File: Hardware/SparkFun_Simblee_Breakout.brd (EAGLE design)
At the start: 22.9 x 58.4 mm, 24 parts, among them U1 ADP160, U2 RFD77101

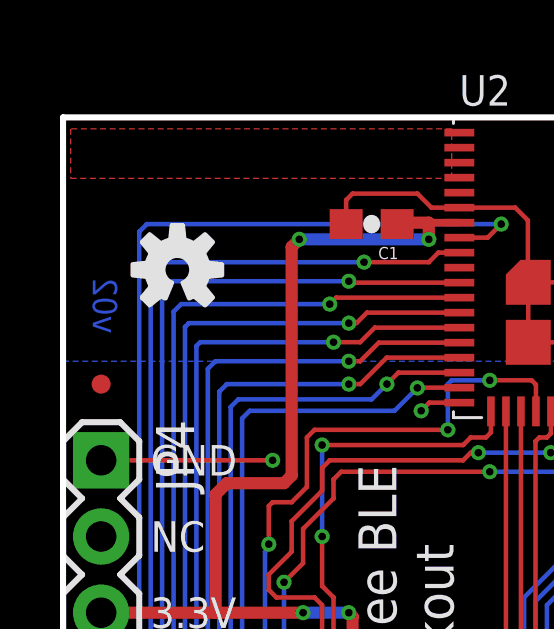
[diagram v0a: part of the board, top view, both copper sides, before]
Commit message: Update to v10. Chg gnd pad to 12.5% paste
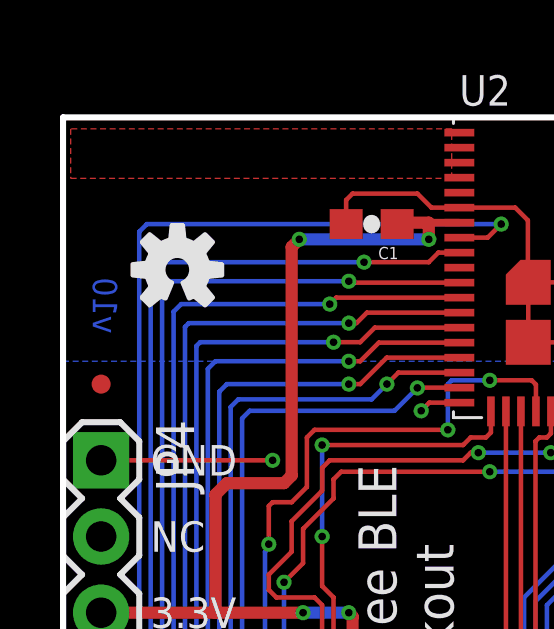
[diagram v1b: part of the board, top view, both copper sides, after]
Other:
- board text added: "v10"
- board text removed: "v02"
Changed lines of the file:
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@@
 <layers>
 <layer number="1" name="Top" color="4" fill="1" visible="yes" active="yes"/>
-<layer number="2" name="Route2" color="1" fill="3" visible="no" active="yes"/>
-<layer number="15" name="Route15" color="4" fill="6" visible="no" active="yes"/>
+<layer number="2" name="Route2" color="1" fill="3" visible="yes" active="yes"/>
+<layer number="15" name="Route15" color="4" fill="6" visible="yes" active="yes"/>
 <layer number="16" name="Bottom" color="1" fill="1" visible="yes" active="yes"/>
 <layer number="17" name="Pads" color="2" fill="1" visible="yes" active="yes"/>
@@
 <layer number="23" name="tOrigins" color="15" fill="1" visible="yes" active="yes"/>
 <layer number="24" name="bOrigins" color="15" fill="1" visible="yes" active="yes"/>
-<layer number="25" name="tNames" color="7" fill="1" visible="no" active="yes"/>
-<layer number="26" name="bNames" color="7" fill="1" visible="no" active="yes"/>
-<layer number="27" name="tValues" color="7" fill="1" visible="no" active="yes"/>
-<layer number="28" name="bValues" color="7" fill="1" visible="no" active="yes"/>
-<layer number="29" name="tStop" color="7" fill="3" visible="no" active="yes"/>
-<layer number="30" name="bStop" color="7" fill="6" visible="no" active="yes"/>
-<layer number="31" name="tCream" color="7" fill="4" visible="no" active="yes"/>
-<layer number="32" name="bCream" color="7" fill="5" visible="no" active="yes"/>
-<layer number="39" name="tKeepout" color="4" fill="11" visible="no" active="yes"/>
-<layer number="40" name="bKeepout" color="1" fill="11" visible="no" active="yes"/>
-<layer number="41" name="tRestrict" color="4" fill="10" visible="no" active="yes"/>
-<layer number="42" name="bRestrict" color="1" fill="10" visible="no" active="yes"/>
-<layer number="43" name="vRestrict" color="2" fill="10" visible="no" active="yes"/>
-<layer number="44" name="Drills" color="7" fill="1" visible="no" active="yes"/>
+<layer number="25" name="tNames" color="7" fill="1" visible="yes" active="yes"/>
+<layer number="26" name="bNames" color="7" fill="1" visible="yes" active="yes"/>
+<layer number="27" name="tValues" color="7" fill="1" visible="yes" active="yes"/>
+<layer number="28" name="bValues" color="7" fill="1" visible="yes" active="yes"/>
+<layer number="29" name="tStop" color="7" fill="3" visible="yes" active="yes"/>
+<layer number="30" name="bStop" color="7" fill="6" visible="yes" active="yes"/>
+<layer number="31" name="tCream" color="7" fill="4" visible="yes" active="yes"/>
+<layer number="32" name="bCream" color="7" fill="5" visible="yes" active="yes"/>
+<layer number="39" name="tKeepout" color="4" fill="11" visible="yes" active="yes"/>
+<layer number="40" name="bKeepout" color="1" fill="11" visible="yes" active="yes"/>
+<layer number="41" name="tRestrict" color="4" fill="10" visible="yes" active="yes"/>
+<layer number="42" name="bRestrict" color="1" fill="10" visible="yes" active="yes"/>
+<layer number="43" name="vRestrict" color="2" fill="10" visible="yes" active="yes"/>
+<layer number="44" name="Drills" color="7" fill="1" visible="yes" active="yes"/>
 <layer number="45" name="Holes" color="7" fill="1" visible="yes" active="yes"/>
-<layer number="46" name="Milling" color="3" fill="1" visible="no" active="yes"/>
-<layer number="47" name="Measures" color="7" fill="1" visible="no" active="yes"/>
+<layer number="46" name="Milling" color="3" fill="1" visible="yes" active="yes"/>
+<layer number="47" name="Measures" color="7" fill="1" visible="yes" active="yes"/>
 <layer number="51" name="tDocu" color="6" fill="1" visible="yes" active="yes"/>
 <layer number="50" name="dxf" color="7" fill="1" visible="no" active="no"/>
@@
 <text x="11.43" y="29.21" size="1.27" layer="22" font="vector" ratio="15" rot="MR270" align="center-left">Simblee BLE
 Breakout</text>
-<text x="1.397" y="53.086" size="0.8128" layer="16" font="vector" ratio="15" rot="MR270" align="center-left">v02</text>
+<text x="1.397" y="53.086" size="0.8128" layer="16" font="vector" ratio="15" rot="MR270" align="center-left">v10</text>
 <text x="30.48" y="-20.32" size="1.778" layer="51" font="vector" ratio="15">Mike Hord</text>
 <rectangle x1="12.3698" y1="56.4896" x2="12.7" y2="57.3278" layer="41"/>
@@
 </class>
 </classes>
-<designrules name="Gold_Phoenix_Standard_Spec_2_layer *">
-<description language="en">&lt;b&gt;EAGLE Design Rules&lt;/b&gt;
-&lt;p&gt;
-The default Design Rules have been set to cover
-a wide range of applications. Your particular design
-may have different requirements, so please make the
-necessary adjustments and save your customized
-design rules under a new name.</description>
+<designrules name="SparkFun-2-layer-FAB-LIMIT">
+<description language="en">&lt;b&gt;SparkFun 2 Layer Design Rule Checks - STANDARD/TIGHT/FAB-LIMIT&lt;/b&gt;
+&lt;p&gt;
+These rules have been curated by SparkFuns DFM commitee. After doing much research, communicating with our multiple fab houses, and getting quotes of various designs, we have compiled three DRU files.
+&lt;p&gt;
+&lt;b&gt;STANDARD:&lt;/b&gt; This is more of a &quot;best case scenario&quot; set of limitations. If your design has the space, and/or you have the time to work within these parameters, please do. Larger trace width and clearance makes for easier visual inspection of the PCB while troubleshooting (useful in production and to the end user). It also allows for better ability to hack a trace (if you are crazy enough to scrape away the mask and solder to a trace). Another thing to keep in mind is that more metal is just more robust.
+&lt;p&gt;
+&lt;b&gt;TIGHT:&lt;/b&gt; This is where cost comes into play. We have found that most fab houses begin to add extra charges when you go smaller than these specs. In some cases, going to less than 15 mil trace can increase the cost by 10%. (This is why we have set the min drill on this DRU to 15 mil) Same story for traces thinner than 7 mil. To avoid those extra charges, then stay within the rules of this DRU.
+&lt;p&gt;
+&lt;b&gt;FAB-LIMIT:&lt;/b&gt; These set of rules are at the very limit of most fab houses capabilities. You will pay more for these specs, and it should be used on designs that have a darned good reason to need 4 mil vias and 4 mil traces.
+&lt;p&gt;
+**NOTE Clearance, Distance, Sizes, and Restring are all set to different limits in each of these three DRU files. Please compare the files within the CAM job editor window of eagle to see all the numbers.
+&lt;p&gt;
+***NOTE, Please set your Net Classes to default (0mil for all settings), so that it won't effect the DRC when you run it with these settings.</description>
 <param name="layerSetup" value="(1*16)"/>
 <param name="mtCopper" value="0.035mm 0.035mm 0.035mm 0.035mm 0.035mm 0.035mm 0.035mm 0.035mm 0.035mm 0.035mm 0.035mm 0.035mm 0.035mm 0.035mm 0.035mm 0.035mm"/>
 <param name="mtIsolate" value="1.5mm 0.15mm 0.2mm 0.15mm 0.2mm 0.15mm 0.2mm 0.15mm 0.2mm 0.15mm 0.2mm 0.15mm 0.2mm 0.15mm 0.2mm"/>
-<param name="mdWireWire" value="7mil"/>
-<param name="mdWirePad" value="7mil"/>
-<param name="mdWireVia" value="7mil"/>
-<param name="mdPadPad" value="7mil"/>
-<param name="mdPadVia" value="7mil"/>
-<param name="mdViaVia" value="7mil"/>
-<param name="mdSmdPad" value="5mil"/>
-<param name="mdSmdVia" value="5mil"/>
-<param name="mdSmdSmd" value="5mil"/>
+<param name="mdWireWire" value="4mil"/>
+<param name="mdWirePad" value="4mil"/>
+<param name="mdWireVia" value="4mil"/>
+<param name="mdPadPad" value="4mil"/>
+<param name="mdPadVia" value="4mil"/>
+<param name="mdViaVia" value="4mil"/>
+<param name="mdSmdPad" value="4mil"/>
+<param name="mdSmdVia" value="4mil"/>
+<param name="mdSmdSmd" value="4mil"/>
 <param name="mdViaViaSameLayer" value="8mil"/>
 <param name="mnLayersViaInSmd" value="2"/>
-<param name="mdCopperDimension" value="8mil"/>
-<param name="mdDrill" value="8mil"/>
+<param name="mdCopperDimension" value="4mil"/>
+<param name="mdDrill" value="4mil"/>
 <param name="mdSmdStop" value="0mil"/>
-<param name="msWidth" value="5mil"/>
+<param name="msWidth" value="4mil"/>
 <param name="msDrill" value="6mil"/>
 <param name="msMicroVia" value="9.99mm"/>
@@
 <param name="rlMinPadTop" value="5mil"/>
 <param name="rlMaxPadTop" value="20mil"/>
-<param name="rlMinPadInner" value="10mil"/>
+<param name="rlMinPadInner" value="6mil"/>
 <param name="rlMaxPadInner" value="20mil"/>
 <param name="rlMinPadBottom" value="5mil"/>
@@
 <param name="rlMinViaOuter" value="5mil"/>
 <param name="rlMaxViaOuter" value="20mil"/>
-<param name="rlMinViaInner" value="10mil"/>
+<param name="rlMinViaInner" value="6mil"/>
 <param name="rlMaxViaInner" value="20mil"/>
 <param name="rlMinMicroViaOuter" value="4mil"/>

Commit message: Rotate SF logo on bottom, ver to 11
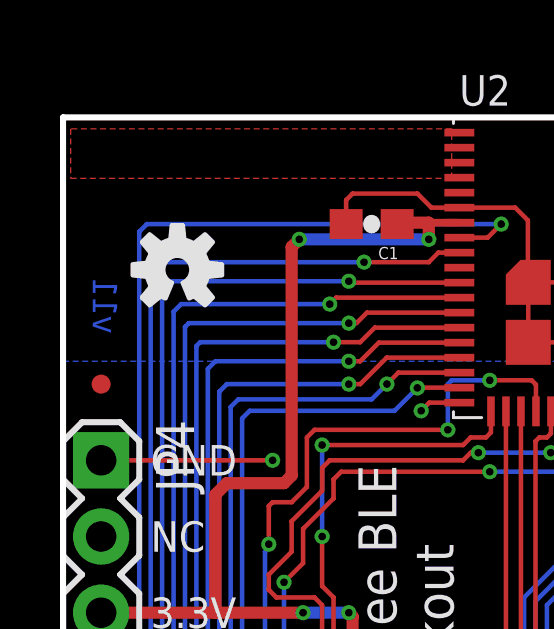
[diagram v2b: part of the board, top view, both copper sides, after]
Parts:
- moved LOGO3 13.7 mm to (13.6, 16.6), turned to 90 degrees
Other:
- board text added: "v11"
- board text removed: "v10"
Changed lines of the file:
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@@
 <grid distance="0.05" unitdist="inch" unit="inch" style="lines" multiple="1" display="yes" altdistance="0.005" altunitdist="inch" altunit="inch"/>
 <layers>
-<layer number="1" name="Top" color="4" fill="1" visible="yes" active="yes"/>
-<layer number="2" name="Route2" color="1" fill="3" visible="yes" active="yes"/>
-<layer number="15" name="Route15" color="4" fill="6" visible="yes" active="yes"/>
+<layer number="1" name="Top" color="4" fill="1" visible="no" active="yes"/>
+<layer number="2" name="Route2" color="1" fill="3" visible="no" active="yes"/>
+<layer number="15" name="Route15" color="4" fill="6" visible="no" active="yes"/>
 <layer number="16" name="Bottom" color="1" fill="1" visible="yes" active="yes"/>
 <layer number="17" name="Pads" color="2" fill="1" visible="yes" active="yes"/>
@@
 <layer number="19" name="Unrouted" color="6" fill="1" visible="yes" active="yes"/>
 <layer number="20" name="Dimension" color="15" fill="1" visible="yes" active="yes"/>
-<layer number="21" name="tPlace" color="16" fill="1" visible="yes" active="yes"/>
+<layer number="21" name="tPlace" color="16" fill="1" visible="no" active="yes"/>
 <layer number="22" name="bPlace" color="14" fill="1" visible="yes" active="yes"/>
-<layer number="23" name="tOrigins" color="15" fill="1" visible="yes" active="yes"/>
+<layer number="23" name="tOrigins" color="15" fill="1" visible="no" active="yes"/>
 <layer number="24" name="bOrigins" color="15" fill="1" visible="yes" active="yes"/>
-<layer number="25" name="tNames" color="7" fill="1" visible="yes" active="yes"/>
-<layer number="26" name="bNames" color="7" fill="1" visible="yes" active="yes"/>
-<layer number="27" name="tValues" color="7" fill="1" visible="yes" active="yes"/>
-<layer number="28" name="bValues" color="7" fill="1" visible="yes" active="yes"/>
-<layer number="29" name="tStop" color="7" fill="3" visible="yes" active="yes"/>
-<layer number="30" name="bStop" color="7" fill="6" visible="yes" active="yes"/>
-<layer number="31" name="tCream" color="7" fill="4" visible="yes" active="yes"/>
-<layer number="32" name="bCream" color="7" fill="5" visible="yes" active="yes"/>
-<layer number="39" name="tKeepout" color="4" fill="11" visible="yes" active="yes"/>
-<layer number="40" name="bKeepout" color="1" fill="11" visible="yes" active="yes"/>
-<layer number="41" name="tRestrict" color="4" fill="10" visible="yes" active="yes"/>
-<layer number="42" name="bRestrict" color="1" fill="10" visible="yes" active="yes"/>
-<layer number="43" name="vRestrict" color="2" fill="10" visible="yes" active="yes"/>
-<layer number="44" name="Drills" color="7" fill="1" visible="yes" active="yes"/>
-<layer number="45" name="Holes" color="7" fill="1" visible="yes" active="yes"/>
-<layer number="46" name="Milling" color="3" fill="1" visible="yes" active="yes"/>
-<layer number="47" name="Measures" color="7" fill="1" visible="yes" active="yes"/>
-<layer number="51" name="tDocu" color="6" fill="1" visible="yes" active="yes"/>
+<layer number="25" name="tNames" color="7" fill="1" visible="no" active="yes"/>
+<layer number="26" name="bNames" color="7" fill="1" visible="no" active="yes"/>
+<layer number="27" name="tValues" color="7" fill="1" visible="no" active="yes"/>
+<layer number="28" name="bValues" color="7" fill="1" visible="no" active="yes"/>
+<layer number="29" name="tStop" color="7" fill="3" visible="no" active="yes"/>
+<layer number="30" name="bStop" color="7" fill="6" visible="no" active="yes"/>
+<layer number="31" name="tCream" color="7" fill="4" visible="no" active="yes"/>
+<layer number="32" name="bCream" color="7" fill="5" visible="no" active="yes"/>
+<layer number="39" name="tKeepout" color="4" fill="11" visible="no" active="yes"/>
+<layer number="40" name="bKeepout" color="1" fill="11" visible="no" active="yes"/>
+<layer number="41" name="tRestrict" color="4" fill="10" visible="no" active="yes"/>
+<layer number="42" name="bRestrict" color="1" fill="10" visible="no" active="yes"/>
+<layer number="43" name="vRestrict" color="2" fill="10" visible="no" active="yes"/>
+<layer number="44" name="Drills" color="7" fill="1" visible="no" active="yes"/>
+<layer number="45" name="Holes" color="7" fill="1" visible="no" active="yes"/>
+<layer number="46" name="Milling" color="3" fill="1" visible="no" active="yes"/>
+<layer number="47" name="Measures" color="7" fill="1" visible="no" active="yes"/>
+<layer number="51" name="tDocu" color="6" fill="1" visible="no" active="yes"/>
 <layer number="50" name="dxf" color="7" fill="1" visible="no" active="no"/>
 <layer number="3" name="Route3" color="4" fill="3" visible="no" active="no"/>
@@
 <text x="11.43" y="29.21" size="1.27" layer="22" font="vector" ratio="15" rot="MR270" align="center-left">Simblee BLE
 Breakout</text>
-<text x="1.397" y="53.086" size="0.8128" layer="16" font="vector" ratio="15" rot="MR270" align="center-left">v10</text>
+<text x="1.397" y="53.086" size="0.8128" layer="16" font="vector" ratio="15" rot="MR270" align="center-left">v11</text>
 <text x="30.48" y="-20.32" size="1.778" layer="51" font="vector" ratio="15">Mike Hord</text>
 <rectangle x1="12.3698" y1="56.4896" x2="12.7" y2="57.3278" layer="41"/>
@@
 <element name="LOGO1" library="SparkFun-Aesthetics" package="SFE_LOGO_NAME_.1" value="SFE_LOGO_NAME.1_INCH" x="8.763" y="19.05" rot="R90"/>
 <element name="LOGO2" library="SparkFun-Aesthetics" package="OSHW-LOGO-S" value="OSHW-LOGOS" x="3.81" y="53.34"/>
-<element name="LOGO3" library="SparkFun-Aesthetics" package="SFE_LOGO_NAME_.1" value="SFE_LOGO_NAME.1_INCH" x="17.653" y="29.718" rot="MR270"/>
+<element name="LOGO3" library="SparkFun-Aesthetics" package="SFE_LOGO_NAME_.1" value="SFE_LOGO_NAME.1_INCH" x="13.589" y="16.637" rot="MR90"/>
 <element name="LOGO4" library="SparkFun-Aesthetics" package="OSHW-LOGO-S" value="OSHW-LOGOS" x="3.81" y="53.34" rot="MR0"/>
 <element name="D1" library="SparkFun-DiscreteSemi" package="SOD-523" value="RB751" x="8.89" y="12.954" rot="R180">
